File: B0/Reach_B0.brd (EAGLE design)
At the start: 107.3 x 69.5 mm, 150 parts, among them IC1 TMC2100-LA, IC18 74AHC1G126DCK, IC2 TMC2100-LA, IC3 74AHC1G126DCK, IC4 74AHC1G126DCK, IC5 74AHC1G126DCK, IC6 74AHC1G126DCK, IC7 74AHC1G126DCK, P8 F-2X23-, P9 F-2X23-, Q2 AON6758, Q3 AON6758, U1 SN74AHC595PW, U10 RT8268, U11 PCA9685PW, U18 CAT24C256, U2 SN74AHC595PW, U3 MCP9600, U4 MCP9600, U5 MCP9600, U6 MCP9600, X1 22-05-7028-02, X11 22-05-7028-02, X14 22-05-7048-04, X2 MSTBA4, X21 MSTBA2, X3 MSTBA2, X4 22-05-7028-02, X5 22-05-7028-02, X6 22-05-7048-04, X7 22-05-7028-02, X9 22-05-7028-02

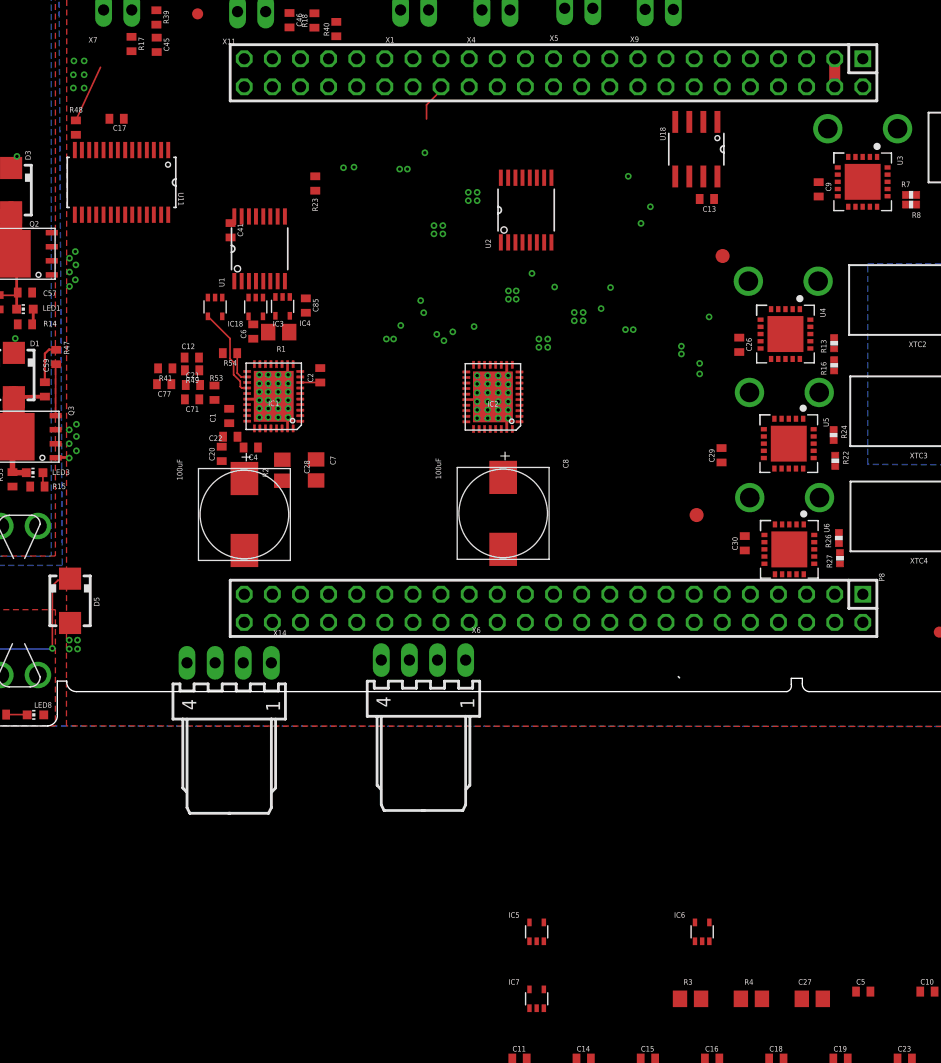
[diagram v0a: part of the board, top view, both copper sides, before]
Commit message: multisheet schematic changes
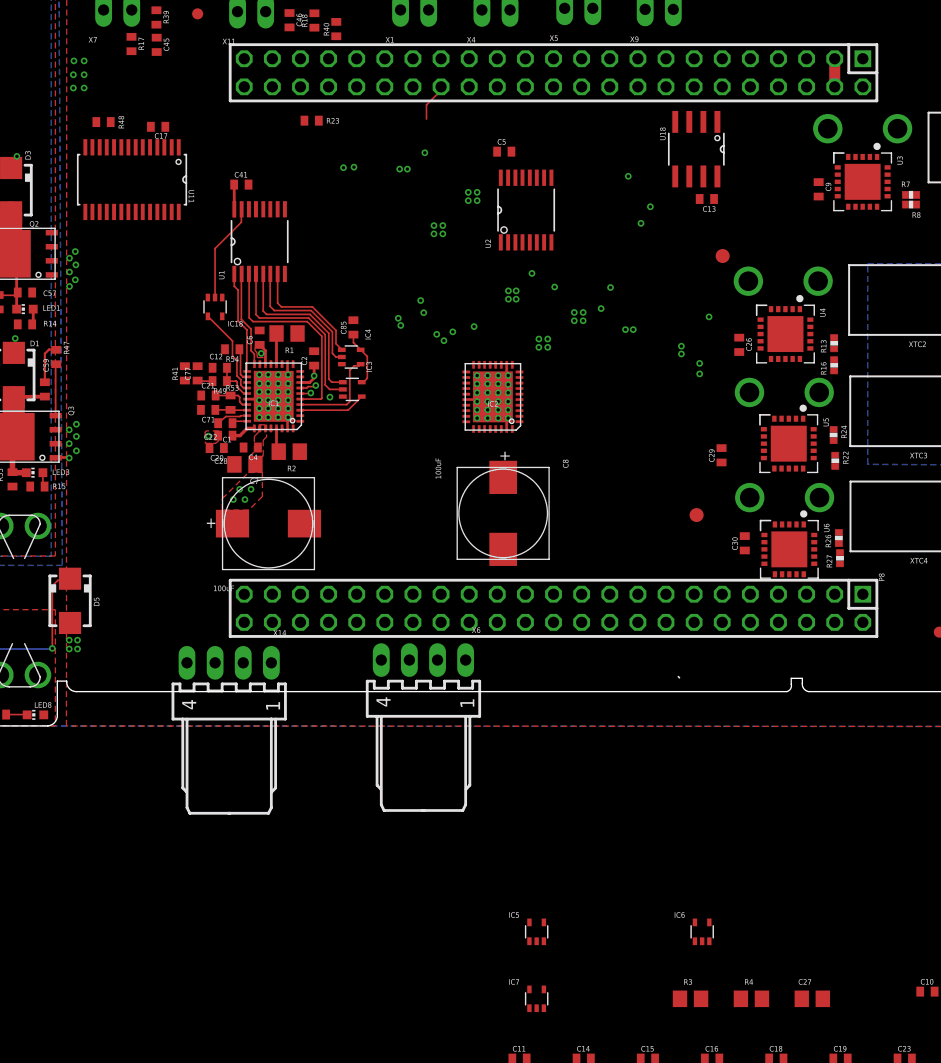
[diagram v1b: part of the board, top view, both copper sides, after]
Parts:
- R13, R22, R26: value (none) -> 10k
- R16: value (none) -> 2.2k
- R24: value (none) -> 4.3k
- R27: value (none) -> 7.5k
- R7: value (none) -> DNP
- R8: value (none) -> 0
- moved C5 82.5 mm to (53.9, 51.9)
- moved IC3 11.5 mm to (40.2, 30.4), turned to 270 degrees
- moved IC4 7.71 mm to (40.1, 33.3), turned to 270 degrees
- moved C7 6.44 mm to (30.5, 23.6), turned to 180 degrees
- moved R23 5.68 mm to (36.5, 54.7), turned to 0 degrees
- moved C85 4.73 mm to (40.3, 36.0), turned to 90 degrees
- moved C41 4.24 mm to (30.2, 48.9), turned to 0 degrees
- moved C17 3.82 mm to (22.7, 54.1)
- moved C77 3.18 mm to (26.2, 31.9), turned to 90 degrees
- moved C12 2.69 mm to (28.2, 32.4)
- moved R49 2.68 mm to (28.2, 31.1)
- moved R48 2.55 mm to (17.7, 54.5), turned to 0 degrees
- moved C28 2.33 mm to (32.6, 18.3), turned to 0 degrees
- moved R41 1.83 mm to (25.1, 31.9), turned to 90 degrees
- moved R2 1.79 mm to (34.5, 24.8), turned to 180 degrees
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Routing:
- net N$44: track 0.00 -> 18.8 mm
- net N$34: track 0.00 -> 17.0 mm
- net N$40: track 0.00 -> 15.6 mm
- net N$5: track 0.00 -> 12.4 mm
- net N$4: track 0.00 -> 10.9 mm
- net N$43: track 0.00 -> 9.28 mm
- net N$120: track 0.00 -> 8.96 mm
- net +3V3: track 4.36 -> 13.1 mm, vias 0 -> 1
- net N$6: track 0.00 -> 8.64 mm
- net X_CFG1: track 0.00 -> 8.62 mm
- net X_CFG2: track 0.00 -> 6.06 mm
- net HEATER_B: track 5.29 -> 0.00 mm
- net N$20: track 0.00 -> 3.80 mm
- net N$31: track 0.00 -> 3.44 mm
- net N$108: track 0.00 -> 2.89 mm
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
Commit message: stepper drivers laid out
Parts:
- added C31, C34, C37, C40: 4.7uF, rcl:C0402
- added C32: 22nF, rcl:C0402
- added C33, C35, C36, C38, C39, C42, C43, C44: 0.1uF, rcl:C0402
- added C47: 10uF, rcl:C0805
- added C48: 100uF, Panasonic-EEEFK_EEEFP:RHS1V10MCN1GS
- added IC10, IC11, IC9: 74AHC1G126DCK, 74xx-little-de:SC70-5
- added IC8: TMC2100-LA, we-chip:QFN36-PAD
- added R28: 10k, rcl:R0402
- added R29: 7.5k, rcl:R0402
- added R30: 4.3k, rcl:R0402
- added R31, R35: 0.1R, rcl:R0805
- added R36, R46: 10K, rcl:R0402
- added R37: 4.7K, rcl:R0402
- added R38: 2.2R, rcl:R0402
- added U7: SN74AHC595PW, sn74hc595:SOP65P640X120-16N
- added X8: 22-05-7048-04, con-molex:7395-04
- moved R12 81.3 mm to (38.6, 33.9), turned to 90 degrees
- moved R6 80.1 mm to (40.7, 30.9), turned to 180 degrees
- moved R9 77.1 mm to (41.8, 33.8), turned to 180 degrees
- moved C19 76.7 mm to (38.7, 31.6), turned to 90 degrees
- moved C10 76.1 mm to (40.7, 32.1), turned to 180 degrees
- moved C23 75.6 mm to (52.8, 35.8), turned to 90 degrees
- moved C25 71.6 mm to (44.3, 34.8), turned to 90 degrees
- moved R10 70.7 mm to (41.7, 28.9), turned to 270 degrees
- moved C18 70.1 mm to (39.6, 28.3), turned to 180 degrees
- moved C3 67.0 mm to (41.2, 27.1), turned to 180 degrees
- moved C15 65.6 mm to (39.7, 29.6)
- moved IC7 64.7 mm to (39.9, 37.8), turned to 90 degrees
- moved R3 64.5 mm to (46.8, 35.2), turned to 180 degrees
- moved C16 64.3 mm to (41.2, 26.0), turned to 180 degrees
- moved C11 63.3 mm to (49.2, 33.0), turned to 90 degrees
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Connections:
- removed net THERMO_1: P9.37
- new net DIR_C: IC8.7, P9.29
- new net ENABLE_C: IC11.4, IC8.22
- new net IREF_C_RAW: R46.2, U11.20
- new net IREF_X2: C40.1, R36.2, R46.1
- new net N$52: C32.2, IC8.27
- new net N$53: R29.1, R30.2
- new net N$54: IC8.14, R31.2
- new net N$55: IC8.33, R35.2
- new net N$56: C34.1, IC8.23, R36.1
- new net N$57: C32.1, IC8.28
- new net N$58: C37.2, IC8.25, R38.1
- new net N$59: C38.1, IC8.29
- new net N$60: IC8.18, U7.2
- new net N$61: IC8.19, U7.1
- new net N$62: IC10.1, U7.7
- new net N$63: IC10.2, U7.6
- new net N$65: IC9.2, U7.4
- new net N$66: IC9.1, U7.5
- new net N$67: IC8.5, U7.3
- new net N$68: C39.1, IC8.26, R38.2
- new net N$69: IC11.2, U7.15
- new net N$9: C17.1, U11.28
- new net STEP_C: IC8.6, P9.21
- new net X_A5: IC8.34, X8.2
- new net X_A6: IC8.32, X8.1
- new net X_B5: IC8.15, X8.4
- new net X_B6: IC8.13, X8.3
- new net X_CFG5: IC8.3, IC9.4
- new net X_CFG6: IC10.4, IC8.4
- net +3V3: now also C33.1, C35.1, C42.1, IC10.5, IC11.5, IC8.8, IC9.5, R37.2, U7.10, U7.16
- net DIR_A: now also IC1.7; no longer IC2.7
- net DIR_B: now also IC2.7; no longer IC1.7
- net FAULT_REACH: now also C31.1, P9.37, R28.1, R29.2; no longer P9.21
- net FAULT_X: now also IC8.20, R28.2, R37.1
- net GND: now also C31.2, C33.2, C34.2, C35.2, C36.1, C37.1, C39.2, C40.2, C42.2, C43.2, C44.2, C47.2, C48.-, IC10.3, IC11.3, IC8.1, IC8.10, IC8.11, IC8.12, IC8.24, IC8.35, IC8.36, IC8.TP, IC9.3, R30.1, R31.1, R35.1, U7.13, U7.8
- net IREF_A_RAW: now also R41.2; no longer R12.2
- net IREF_B_RAW: now also R12.2; no longer R41.2
- net SER_2: now also U7.9
- net SPI1_CS0: now also U7.12; no longer P9.27
- net SPI1_MOSI: now also U7.14
- net SPI1_SCLK: now also U7.11
- net STEP_A: now also IC1.6; no longer IC2.6
- net STEP_B: now also IC2.6; no longer IC1.6
- net TRISTATE_STEPPERS: now also IC11.1
- net VDD_5V: no longer C17.1, U11.28
- net VDD_IN: now also C36.2, C38.2, C43.1, C44.1, C47.1, C48.+, IC8.16, IC8.30, IC8.31
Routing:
- net +3V3: track 13.1 -> 67.2 mm, vias 1 -> 3
- net N$234: track 31.2 -> 8.21 mm
- net N$67: track 0.00 -> 16.3 mm
- net N$35: track 0.00 -> 16.3 mm
- net N$30: track 0.00 -> 14.6 mm
- net N$65: track 0.00 -> 14.6 mm
- net N$66: track 0.00 -> 13.4 mm
- net N$32: track 0.00 -> 13.4 mm
- net ENABLE_A: track 8.14 -> 20.1 mm
- net VDD_IN: track 22.2 -> 33.5 mm, vias 11 -> 23
- net N$64: track 31.6 -> 20.4 mm
- net N$29: track 0.00 -> 10.4 mm
- net N$63: track 0.00 -> 10.4 mm
- net ENABLE_C: track 0.00 -> 10.1 mm
- net N$28: track 0.00 -> 9.07 mm
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- added copper zone on layer 1, net N$234
- added copper zone on layer 1, net N$64
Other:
- board text added: "C"

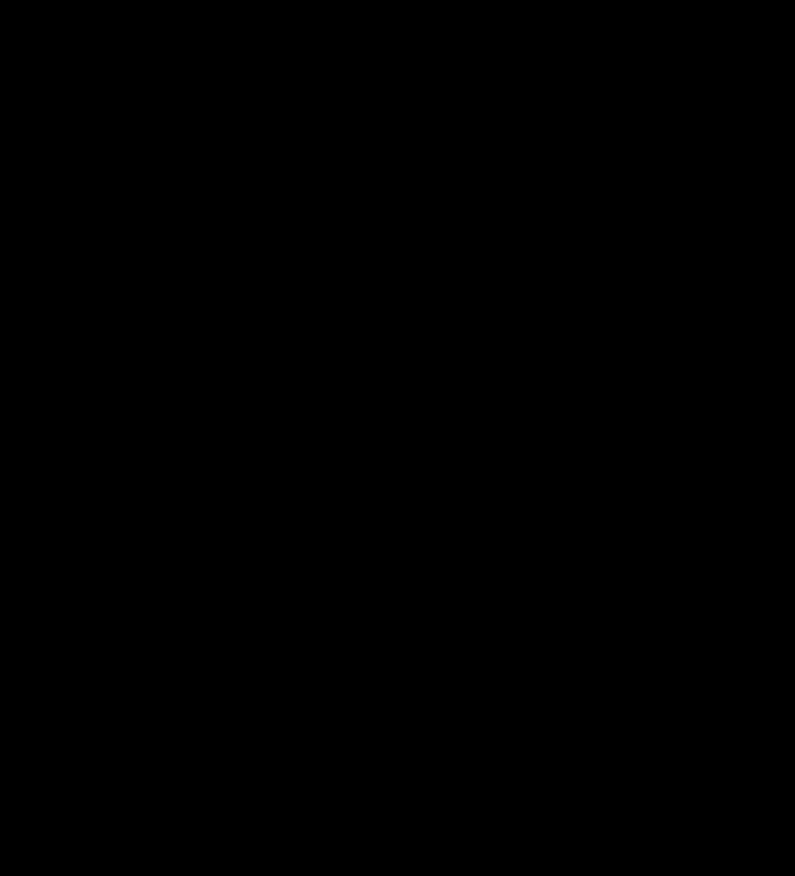
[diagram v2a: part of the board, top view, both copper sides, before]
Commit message: example layout of esd and low pass filter added to thermocouple1
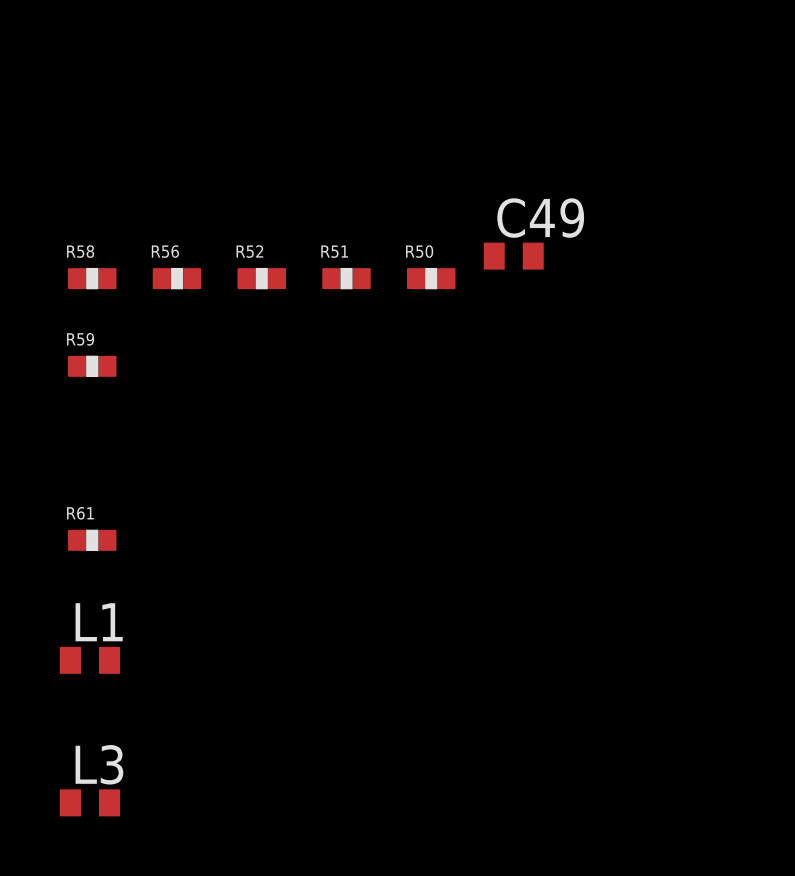
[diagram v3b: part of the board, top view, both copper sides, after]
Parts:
- added C49: 0.1uF, rcl:C0402
- added L1, L3: BLM15HB121SN1, inductors:0402
- added R50, R51, R52, R56, R58, R59, R61: 10k, SparkFun-Resistors:0402-RES
- R7: value DNP -> 10k
- R8: value 0 -> 2.2k
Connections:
- new net N$11: L3.1, R50.2, R51.1, R56.1
- new net N$51: R50.1, R52.2
- new net N$70: C49.2, R56.2, U3.P$2
- new net N$71: C49.1, R58.2, U3.P$4
- new net N$72: L1.1, R58.1, R59.2
- new net N$73: R59.1, R61.2
- net GND: now also R52.1, R61.1
- net N$14: now also L3.2; no longer U3.P$2
- net N$15: now also L1.2; no longer U3.P$4
- net VDD_5V: now also R51.2

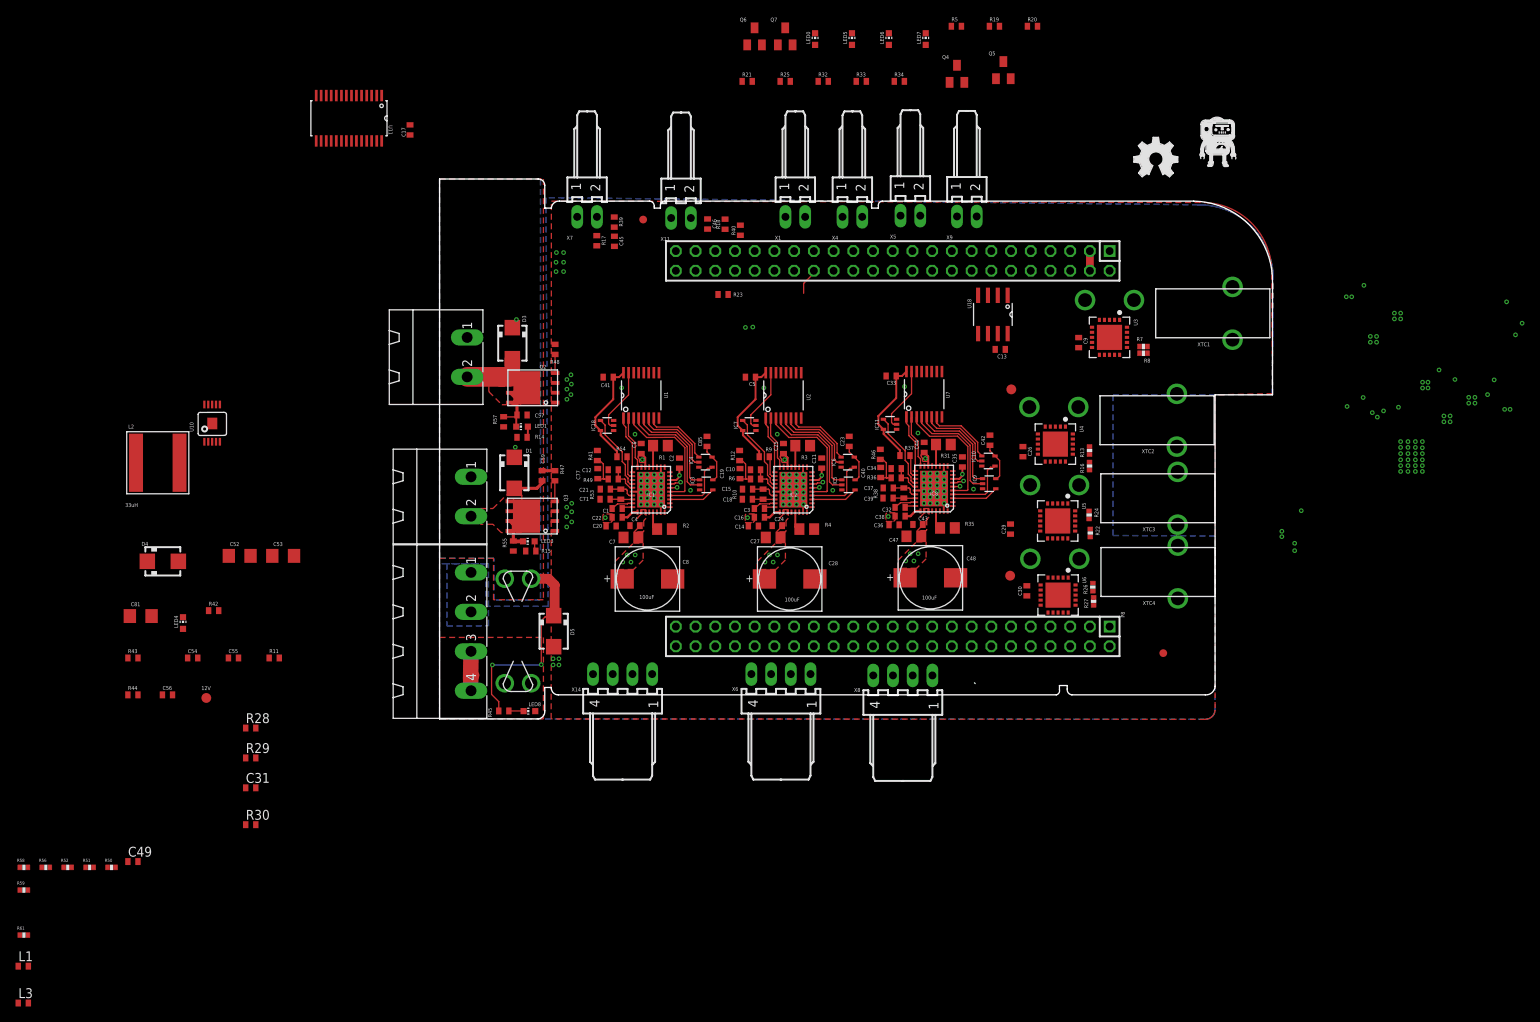
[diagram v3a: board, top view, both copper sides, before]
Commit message: supply layout complete
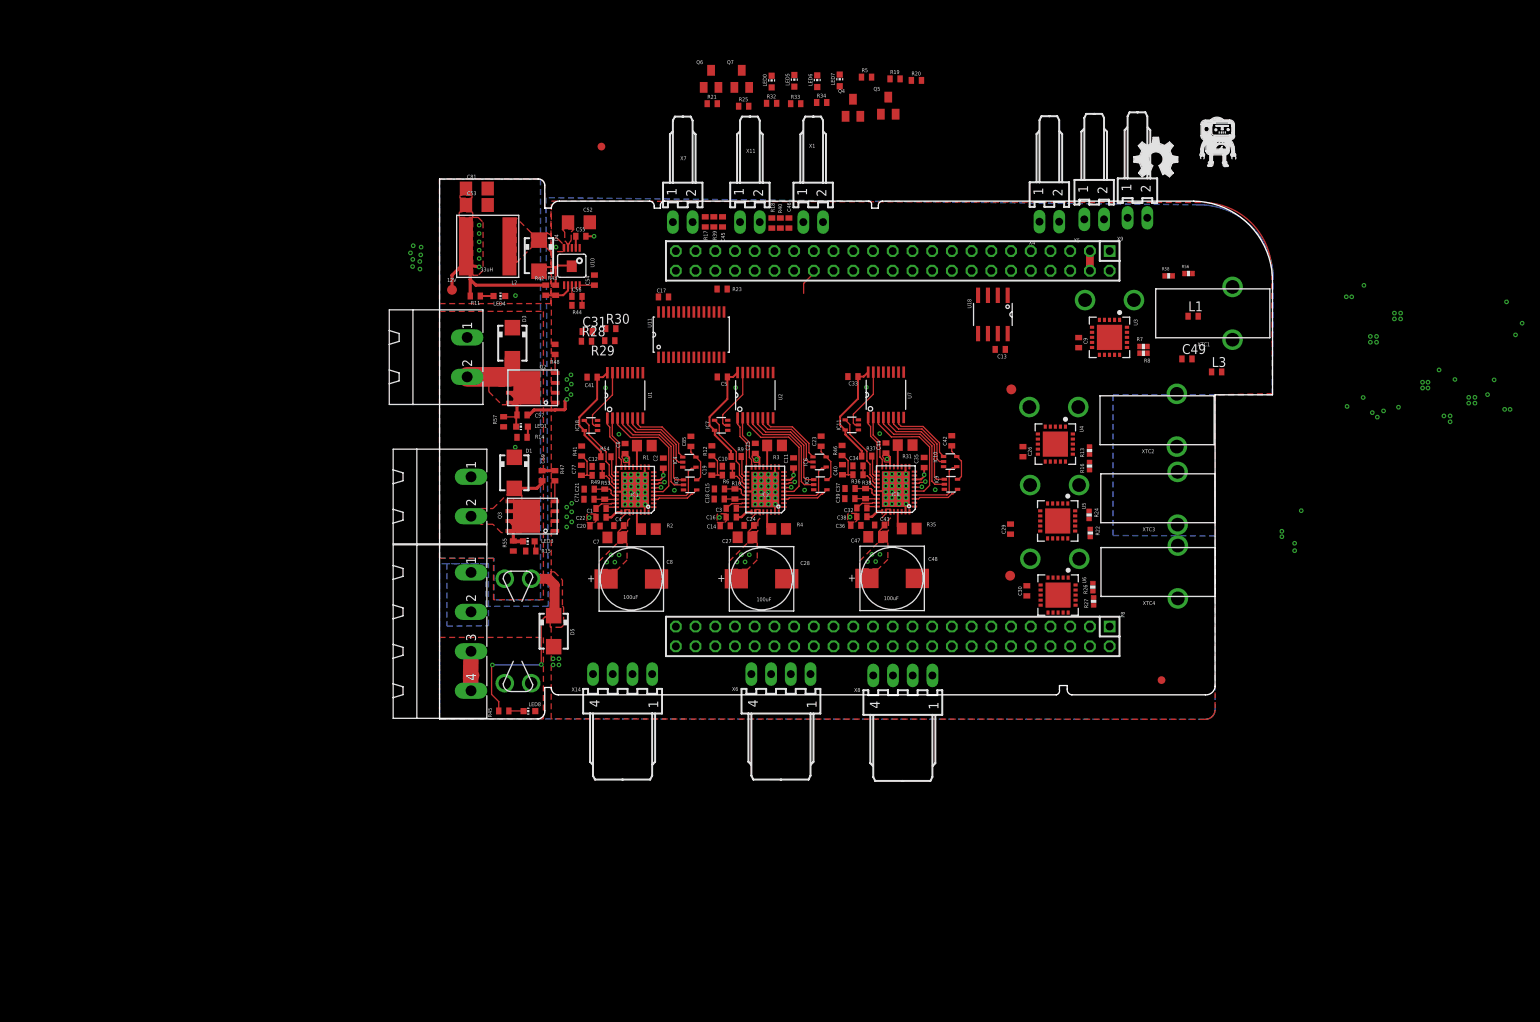
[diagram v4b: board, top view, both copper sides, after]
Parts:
- removed R50, R51, R52, R59, R61: 10k, SparkFun-Resistors:0402-RES
- R56, R58: value 10k -> 100
- R7: value 10k -> DNP
- R8: value 2.2k -> 0
- moved L3 173.9 mm to (100.1, 44.7)
- moved L1 172.4 mm to (97.1, 51.9)
- moved R58 166.0 mm to (93.9, 57.1)
- moved R56 165.9 mm to (96.5, 57.4)
- moved C49 150.4 mm to (96.3, 46.4)
- moved R30 79.0 mm to (22.1, 50.3)
- moved R44 76.1 mm to (17.7, 53.3), turned to 180 degrees
- moved C56 73.6 mm to (17.7, 54.4)
- moved C31 73.0 mm to (19.0, 49.9)
- moved R43 72.2 mm to (14.9, 55.2), turned to 90 degrees
- moved C54 71.0 mm to (19.9, 56.5), turned to 90 degrees
- moved R29 70.9 mm to (21.9, 48.7), turned to 180 degrees
- moved C55 70.4 mm to (18.2, 62.2)
- moved C81 70.1 mm to (4.80, 68.3)
- moved R28 66.0 mm to (18.9, 48.6)
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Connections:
- removed net N$51: R50.1, R52.2
- removed net N$73: R59.1, R61.2
- removed net N$9: C17.1, U11.28
- new net SER_3: U2.9, U7.14
- net GND: no longer R52.1, R61.1
- net N$11: no longer R50.2, R51.1
- net N$72: no longer R59.2
- net SER_2: now also U2.14; no longer U2.9, U7.9
- net SPI1_MOSI: no longer U2.14, U7.14
- net VDD_5V: now also C17.1, U11.28; no longer R51.2
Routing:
- net VDD_12V: track 0.00 -> 19.9 mm, vias 0 -> 6
- net GND: track 8.72 -> 21.3 mm, vias 171 -> 146
- net N$233: track 0.00 -> 3.81 mm
- net N$243: track 0.00 -> 1.90 mm
- net N$96: track 0.00 -> 1.70 mm
- net N$245: track 0.00 -> 1.50 mm
- net N$244: track 0.00 -> 1.45 mm
- net N$246: track 0.00 -> 1.15 mm
- net N$238: track 0.00 -> 1.05 mm, vias 0 -> 2
- added copper zone on layer 1, net N$238
- added copper zone on layer 1, net N$74
- added copper zone on layer 1, net VDD_12V
